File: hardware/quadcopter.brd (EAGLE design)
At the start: 130.1 x 130.1 mm, 99 parts, among them J1 HEADER-4POS-0.1IN-FEMALE-SMD-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, J2 HEADER-10POSTH-254X10, J3 HEADER-4POS-0.1IN-FEMALE, J4 AVR_SPI_PRG_6-SMD, M1 MOTOR_PADS_GND-MOLEX-SMD, M2 MOTOR_PADS_GND-MOLEX-SMD, M3 MOTOR_PADS_GND-MOLEX-SMD, M4 MOTOR_PADS_GND-MOLEX-SMD, P1 PROPELLOR-45MM, P2 PROPELLOR-45MM, P3 PROPELLOR-45MM, P4 PROPELLOR-45MM, Q1 N-MOSFET-SI2302DS, Q12 N-MOSFET-SI2302DS, Q2 N-MOSFET-SI2302DS, Q3 N-MOSFET-SI2302DS, Q4 N-MOSFET-SI2302DS, Q6 N-MOSFET-SI2302DS, Q8 N-MOSFET-SI2302DS, Q9 N-MOSFET-SI2302DS, SW1 PUSHBUTTON_-4.5X4.5, U1 ATMEGA128RFA1, U2 IMU_LSM9DS1-LSM9DS1, Y1 CRYSTAL5X3

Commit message: Replaced local refs to `custom_michael_shao` lbr with team version
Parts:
- DEC1: value TIE Fighter -> DECORATION-TIE_FIGHTER_0.15_SCALE

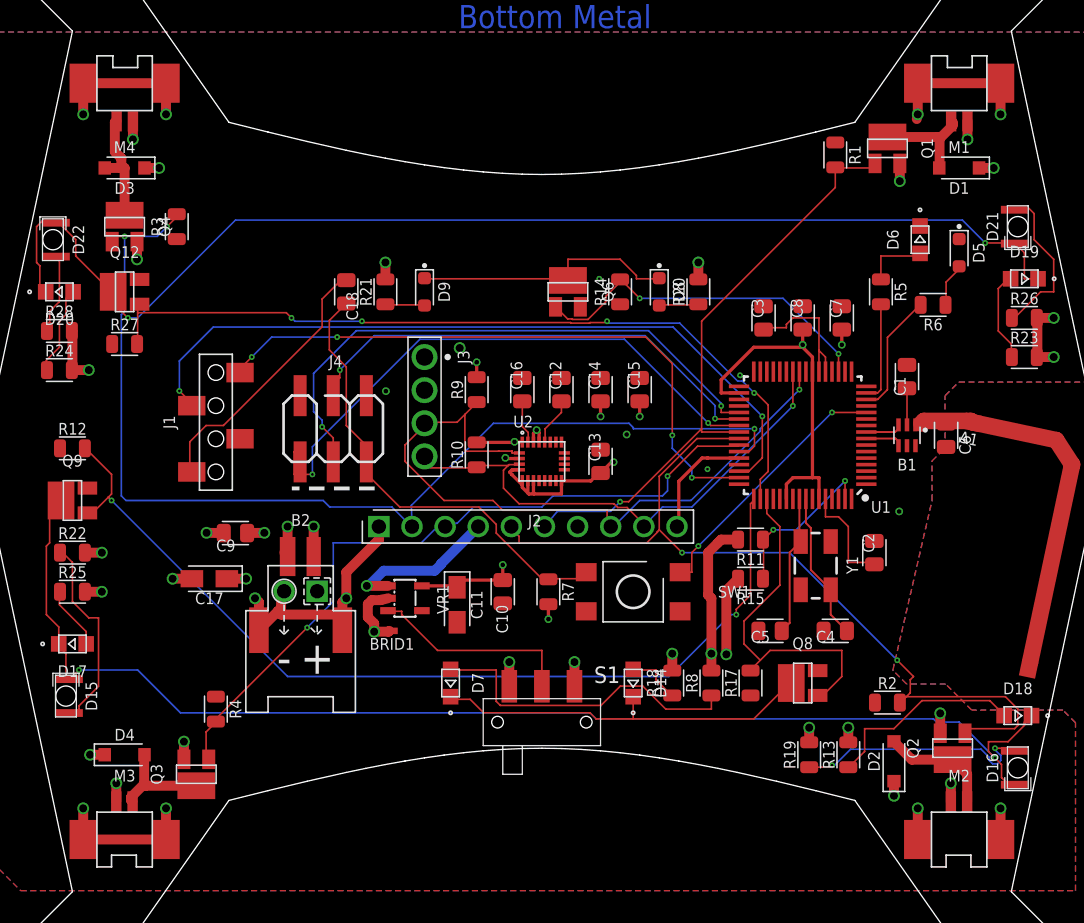
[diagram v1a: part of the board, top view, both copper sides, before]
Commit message: Cleaned up `BAT_GND` traces
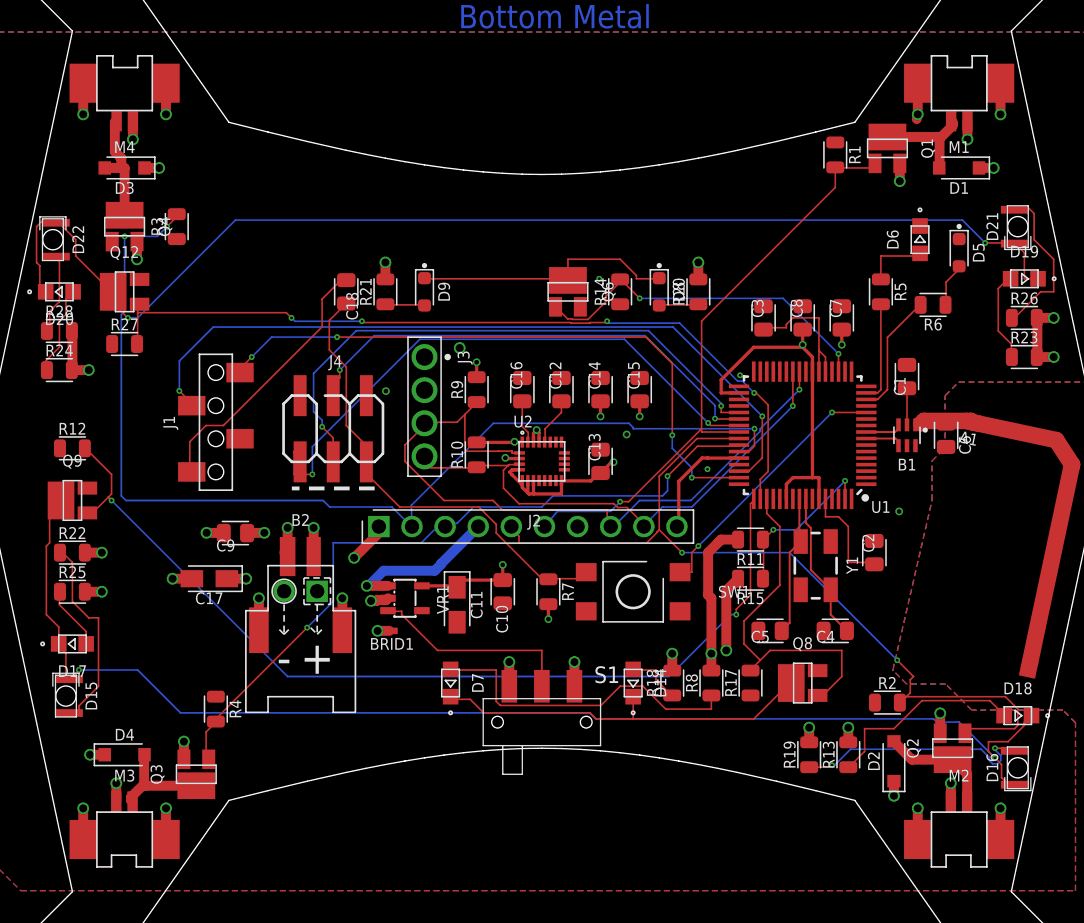
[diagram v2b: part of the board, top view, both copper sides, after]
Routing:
- net BAT_GND: track 85.4 -> 49.5 mm, vias 20 -> 22
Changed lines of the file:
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@@
 <setting verticaltext="up"/>
 </settings>
-<grid distance="0.5" unitdist="mm" unit="mm" style="lines" multiple="1" display="yes" altdistance="0.1" altunitdist="mm" altunit="mm"/>
+<grid distance="0.1" unitdist="mm" unit="mm" style="lines" multiple="1" display="yes" altdistance="0.1" altunitdist="mm" altunit="mm"/>
 <layers>
 <layer number="1" name="Top" color="4" fill="1" visible="yes" active="yes"/>
@@
 <via x="28.825" y="-26.6096" extent="1-16" drill="0.6096"/>
 <via x="35.175" y="-26.6096" extent="1-16" drill="0.6096"/>
-<wire x1="-19.5" y1="-7.3" x2="-19.5" y2="-5" width="0.762" layer="1"/>
-<via x="-19.5" y="-5" extent="1-16" drill="0.6096"/>
-<wire x1="-21.7" y1="-12.95" x2="-21.7" y2="-10.8" width="0.762" layer="1"/>
-<wire x1="-21.7" y1="-10.8" x2="-22" y2="-10.5" width="0.762" layer="1"/>
-<via x="-22" y="-10.5" extent="1-16" drill="0.6096"/>
-<wire x1="-15.3" y1="-12.95" x2="-15.3" y2="-10.8" width="0.762" layer="1"/>
-<wire x1="-15.3" y1="-10.8" x2="-15" y2="-10.5" width="0.762" layer="1"/>
-<via x="-15" y="-10.5" extent="1-16" drill="0.6096"/>
+<wire x1="-19.5" y1="-7.3" x2="-19.5" y2="-5.1" width="0.762" layer="1"/>
+<via x="-19.5" y="-5.1" extent="1-16" drill="0.6096"/>
 <wire x1="28.825" y1="26.6096" x2="28.75" y2="26.25" width="0.762" layer="1"/>
-<wire x1="35.175" y1="29" x2="28.825" y2="29" width="0.762" layer="1"/>
-<wire x1="-28.825" y1="29" x2="-35.175" y2="29" width="0.762" layer="1"/>
-<wire x1="-35.175" y1="-29" x2="-28.825" y2="-29" width="0.762" layer="1"/>
-<wire x1="-12.5" y1="-5" x2="-12.5" y2="-6" width="0.762" layer="1"/>
 <wire x1="-26.5" y1="-9" x2="-26.84" y2="-9" width="0.762" layer="1"/>
 <wire x1="-22" y1="-13" x2="-22" y2="-13.25" width="0.762" layer="1"/>
 <wire x1="-22" y1="-13" x2="-21.7" y2="-12.95" width="0.762" layer="1"/>
 <wire x1="-19.75" y1="-7" x2="-19.5" y2="-7.3" width="0.762" layer="1"/>
-<wire x1="-20" y1="-11.25" x2="-20" y2="-10" width="0.762" layer="1"/>
-<wire x1="-21.7" y1="-12.95" x2="-20.25" y2="-11.5" width="0.762" layer="1"/>
-<wire x1="-20.25" y1="-11.5" x2="-20" y2="-11.25" width="0.762" layer="1"/>
-<wire x1="-20" y1="-10" x2="-19.77" y2="-9.96" width="0.762" layer="1"/>
-<wire x1="-20" y1="-11.75" x2="-15.5" y2="-11.75" width="0.762" layer="1"/>
-<wire x1="-15.5" y1="-11.75" x2="-15.3" y2="-12.95" width="0.762" layer="1"/>
-<wire x1="-20" y1="-11.75" x2="-20.25" y2="-11.5" width="0.762" layer="1"/>
-<wire x1="-15" y1="-8.5" x2="-12.5" y2="-6" width="0.762" layer="1"/>
-<wire x1="-15" y1="-10.5" x2="-15" y2="-8.5" width="0.762" layer="1"/>
 <via x="30.55" y="-19.3231" extent="1-16" drill="0.6096"/>
 <wire x1="30.55" y1="-20.85" x2="30.55" y2="-19.3231" width="0.762" layer="1"/>
@@
 </polygon>
 <wire x1="15.045" y1="-9" x2="14.1454" y2="-9.8996" width="0.762" layer="1"/>
-<wire x1="14.1454" y1="-9.8996" x2="14.1454" y2="-14.8" width="0.762" layer="1"/>
-<via x="14.1454" y="-14.8" extent="1-16" drill="0.6096"/>
-<via x="-12.8596" y="-13.0596" extent="1-16" drill="0.6096"/>
-<wire x1="-11.7" y1="-13" x2="-11.7596" y2="-13.0596" width="0.762" layer="1"/>
-<wire x1="-11.7596" y1="-13.0596" x2="-12.8596" y2="-13.0596" width="0.762" layer="1"/>
-<wire x1="-11.8" y1="-10.5" x2="-12.3565" y2="-10.6416" width="0.762" layer="1"/>
-<wire x1="-12.3565" y1="-10.6416" x2="-13.03584375" y2="-10.6416" width="0.762" layer="1"/>
-<wire x1="-13.03584375" y1="-10.6416" x2="-13.3483" y2="-10.95405625" width="0.762" layer="1"/>
-<wire x1="-13.3483" y1="-10.95405625" x2="-13.3483" y2="-11.94594375" width="0.762" layer="1"/>
-<wire x1="-12.8596" y1="-12.43464375" x2="-12.8596" y2="-13.0596" width="0.762" layer="1"/>
-<wire x1="-13.3483" y1="-11.94594375" x2="-12.8596" y2="-12.43464375" width="0.762" layer="1"/>
+<wire x1="14.1454" y1="-9.8996" x2="14.1454" y2="-14.5" width="0.762" layer="1"/>
+<via x="14.1454" y="-14.5" extent="1-16" drill="0.6096"/>
+<wire x1="-12.5" y1="-5" x2="-12.5" y2="-5.5" width="0.762" layer="1"/>
+<wire x1="-12.5" y1="-5.5" x2="-14.4" y2="-7.4" width="0.762" layer="1"/>
+<via x="-14.4" y="-7.4" extent="1-16" drill="0.6096"/>
+<wire x1="-15.3" y1="-12.95" x2="-15.3" y2="-10.5" width="0.762" layer="1"/>
+<via x="-15.3" y="-10.5" extent="1-16" drill="0.6096"/>
+<wire x1="-11.7" y1="-13" x2="-12.6" y2="-13" width="0.762" layer="1"/>
+<via x="-12.6" y="-13" extent="1-16" drill="0.6096"/>
+<via x="-13.1" y="-10.7" extent="1-16" drill="0.6096"/>
+<wire x1="-11.8" y1="-10.5" x2="-11.9416" y2="-10.6416" width="0.762" layer="1"/>
+<wire x1="-11.9416" y1="-10.6416" x2="-12.62094375" y2="-10.6416" width="0.762" layer="1"/>
+<wire x1="-12.62094375" y1="-10.6416" x2="-12.67934375" y2="-10.7" width="0.762" layer="1"/>
+<wire x1="-12.67934375" y1="-10.7" x2="-13.1" y2="-10.7" width="0.762" layer="1"/>
+<wire x1="-21.7" y1="-12.95" x2="-21.7" y2="-10.5" width="0.762" layer="1"/>
+<via x="-21.7" y="-10.5" extent="1-16" drill="0.6096"/>
 </signal>
 <signal name="VBAT" class="3">
@@
 <via x="34.64915" y="22.5" extent="1-16" drill="0.6096"/>
 <via x="-34.7454" y="7" extent="1-16" drill="0.6096"/>
-<wire x1="-17.5" y1="-7.3" x2="-17.5" y2="-5" width="0.762" layer="1"/>
-<via x="-17.5" y="-5" extent="1-16" drill="0.6096"/>
+<wire x1="-17.5" y1="-7.3" x2="-17.5" y2="-5.1" width="0.762" layer="1"/>
+<via x="-17.5" y="-5.1" extent="1-16" drill="0.6096"/>
 <wire x1="-36" y1="7.25" x2="-36" y2="10" width="0.762" layer="1"/>
 <wire x1="-36" y1="10" x2="-36.045" y2="10" width="0.762" layer="1"/>
@@
 <wire x1="-16" y1="-6.25" x2="-16" y2="-10.75" width="0.127" layer="16"/>
 <wire x1="-9.25" y1="-6.25" x2="-16" y2="-6.25" width="0.127" layer="16"/>
-<wire x1="-9.25" y1="-6.25" x2="-8" y2="-5" width="0.127" layer="16"/>
-<wire x1="-8" y1="-5" x2="-7.42" y2="-5" width="0.127" layer="16"/>
+<wire x1="-8" y1="-5" x2="-9.25" y2="-6.25" width="0.127" layer="16"/>
+<wire x1="-7.42" y1="-5" x2="-8" y2="-5" width="0.127" layer="16"/>
 <wire x1="-25" y1="-19.75" x2="-25" y2="-19.955" width="0.127" layer="1"/>
 <via x="-18" y="-12.75" extent="1-16" drill="0.2032"/>

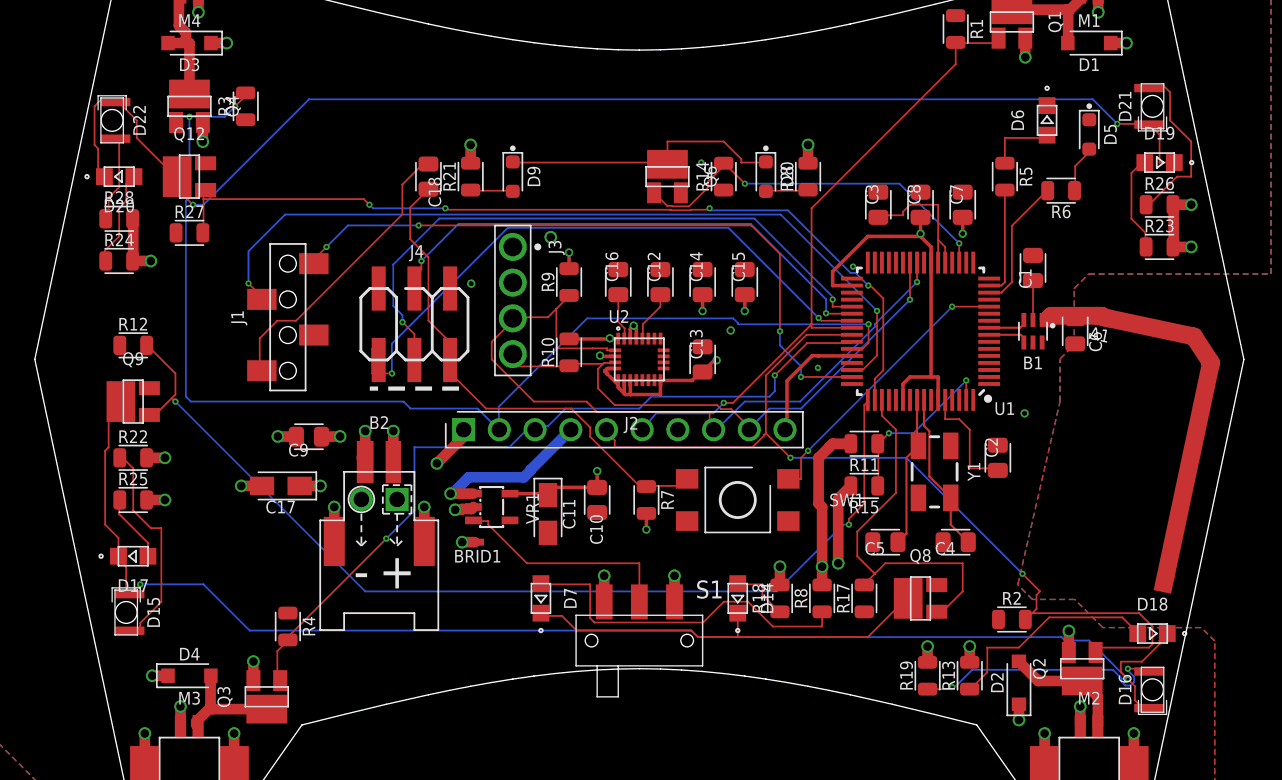
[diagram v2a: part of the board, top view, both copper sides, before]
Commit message: Removed unnecessary LEDs
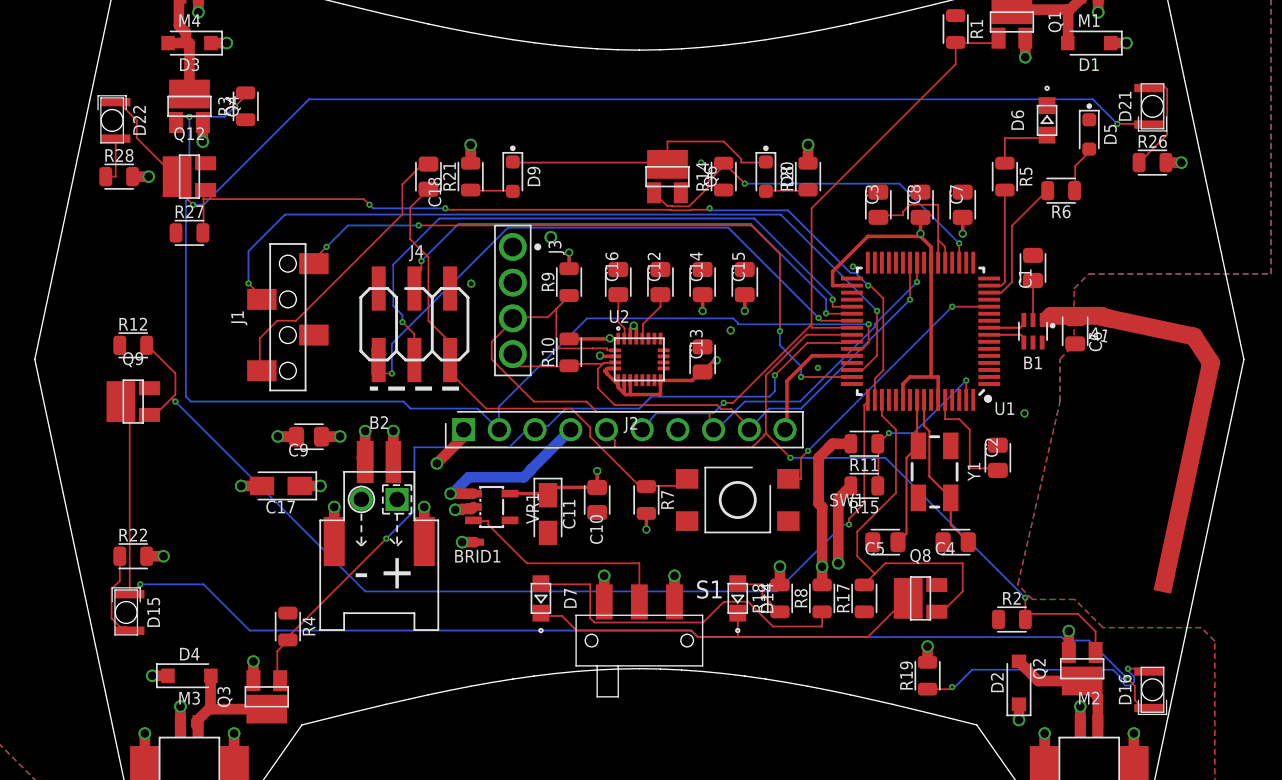
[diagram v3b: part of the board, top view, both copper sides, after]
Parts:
- removed D17, D18, D19, D20: red, custom_michael_shao:LTST-C170EKT
- removed R13, R23, R24, R25: 100, quadparts_prebuilt_2022:RESC2012X60_HS
- moved R22 7.00 mm to (-36.0, -14.0)
- moved R26 3.04 mm to (36.5, 14.0)
- moved R28 3.00 mm to (-37.0, 13.0)
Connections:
- removed net N$24: D17.A, R25.1
- removed net N$25: D18.A, R13.1
- removed net N$38: D19.A, R23.1
- removed net N$39: D20.A, R24.1
- net N$35: no longer D17.C, D18.C
- net N$40: no longer D19.C, D20.C
- net VBAT: no longer R13.2, R23.2, R24.2, R25.2
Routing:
- net N$25: track 15.8 -> 0.00 mm
- net N$40: track 93.4 -> 82.4 mm
- net VBAT: track 59.6 -> 49.7 mm, vias 24 -> 21
- net PWM2: track 65.4 -> 56.2 mm
- net N$34: track 15.3 -> 6.32 mm
- net N$38: track 6.97 -> 0.00 mm
- net N$39: track 6.92 -> 0.00 mm
- net N$35: track 97.8 -> 91.1 mm
- net N$42: track 12.6 -> 7.65 mm
- net N$24: track 4.89 -> 0.00 mm
- net N$43: track 6.42 -> 3.40 mm

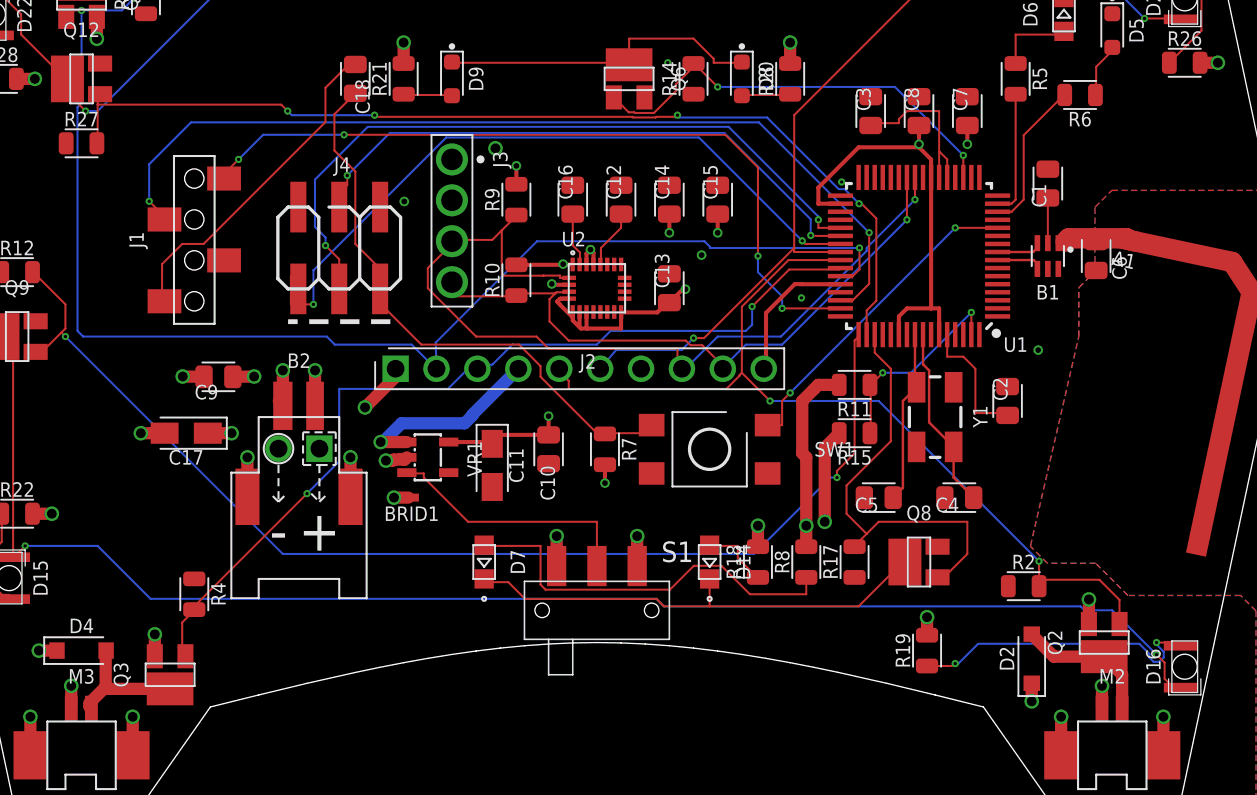
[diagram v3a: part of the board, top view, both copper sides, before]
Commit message: Moved deregulating caps and fixed IMU metal cutouts
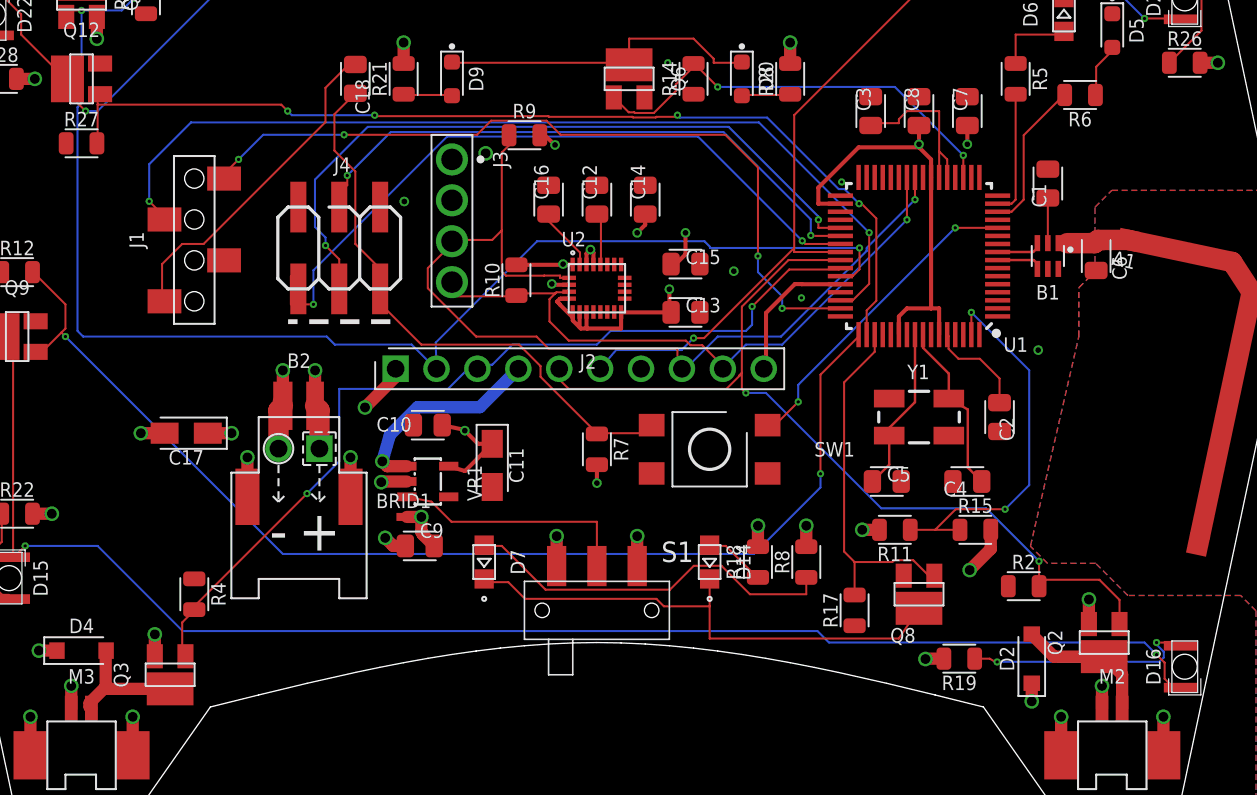
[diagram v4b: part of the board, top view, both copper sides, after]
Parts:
- moved C9 16.3 mm to (-11.0, -16.0), turned to 0 degrees
- moved R15 9.60 mm to (23.5, -15.0), turned to 0 degrees
- moved R11 9.34 mm to (18.5, -15.0)
- moved C10 7.65 mm to (-10.5, -8.50), turned to 180 degrees
- moved C15 4.47 mm to (5.50, 1.50), turned to 0 degrees
- moved R9 4.03 mm to (-4.50, 9.50), turned to 0 degrees
- moved R17 3.00 mm to (16.0, -20.0)
- moved R19 2.06 mm to (22.5, -23.0), turned to 180 degrees
- moved Q8 2.00 mm to (20.0, -19.0), turned to 90 degrees
- moved C13 1.80 mm to (5.50, -1.50), turned to 0 degrees
- moved C12 1.50 mm to (0.00, 5.50)
- moved C14 1.50 mm to (3.00, 5.50)
- moved C16 1.50 mm to (-3.00, 5.50)
- moved VR1 1.50 mm to (-10.5, -12.0)
- moved BRID1 1.30 mm to (-12.0, -14.2), turned to 180 degrees
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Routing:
- net N$28: track 12.6 -> 23.7 mm
- net VBAT: track 49.7 -> 44.2 mm, vias 21 -> 22
- net SCL: track 54.3 -> 59.0 mm
- net N$26: track 18.8 -> 14.8 mm
- net PWM7: track 26.6 -> 22.6 mm
- net ANTENNA: track 7.19 -> 4.43 mm
- net N$27: track 29.8 -> 32.5 mm
- net N$8: track 8.32 -> 6.35 mm
- net N$21: track 25.0 -> 23.6 mm
- net N$23: track 16.3 -> 15.1 mm
- net BAT_GND: track 49.5 -> 50.5 mm, vias 22 -> 21
- net TX0: track 48.5 -> 49.2 mm
- net 2V5: track 69.5 -> 70.2 mm
- net N$22: track 3.33 -> 3.95 mm
- net N$11: track 11.4 -> 10.8 mm
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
